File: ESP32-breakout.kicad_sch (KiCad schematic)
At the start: 39 parts, among them IC1 ESP32-S2-MINI-2U-N4, J1 UJ20-C-H-G-SMT-1-P16-TR, J2 Conn_01x03, J3 Conn_01x19, J4 Conn_01x19, Q2 Q_NMOS_DGS, SW3 SW_MEC_5E, SW4 SW_MEC_5E, U1 STUSB4500QTR, U2 TJA1051T-3, U4 TPSM33606S3QRDNRQ1, U7 MP9361DJ-LF-Z

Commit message: Finished V2 of the PCB
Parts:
- removed C10, C14: 2.2 uF, Capacitor_SMD:C_0603_1608Metric_Pad1.08x0.95mm_HandSolder, symbol Device:C_Small
- removed C11: 0.47 uF, Capacitor_SMD:C_0603_1608Metric_Pad1.08x0.95mm_HandSolder, symbol Device:C_Small
- removed C18: 4.7 uF, Capacitor_SMD:C_0603_1608Metric_Pad1.08x0.95mm_HandSolder, symbol Device:C_Small
- removed C19: 0.1 uF, Capacitor_SMD:C_0603_1608Metric_Pad1.08x0.95mm_HandSolder, symbol Device:C_Small
- removed C20: 1 uF, Capacitor_SMD:C_0603_1608Metric_Pad1.08x0.95mm_HandSolder, symbol Device:C_Small
- removed C21, C22: 22 uF, Capacitor_SMD:C_0603_1608Metric_Pad1.08x0.95mm_HandSolder, symbol Device:C_Small
- removed Q2: Q_NMOS_DGS, Package_TO_SOT_SMD:SOT-23-3, symbol Transistor_FET:Q_NMOS_DGS
- removed R14: 10k, Resistor_SMD:R_0603_1608Metric_Pad0.98x0.95mm_HandSolder, symbol Device:R_Small
- removed R15: 100k, Resistor_SMD:R_0603_1608Metric_Pad0.98x0.95mm_HandSolder, symbol Device:R_Small
- removed R16, R17: 4.7, Resistor_SMD:R_0603_1608Metric_Pad0.98x0.95mm_HandSolder, symbol Device:R_Small
- removed U1: STUSB4500QTR, Package_DFN_QFN:QFN-24-1EP_4x4mm_P0.5mm_EP2.7x2.7mm, symbol Interface_USB:STUSB4500QTR
- removed U4: TPSM33606S3QRDNRQ1, TPSM33606S3QRDNRQ1:TPSM33606S3QRDNRQ1, symbol TPSM33606S3QRDNRQ1:TPSM33606S3QRDNRQ1
- removed U7: MP9361DJ-LF-Z, Jayse_Footprints:TSOT23-6_MP9361_MNP, symbol 2026-06-30_18-02-43:MP9361DJ-LF-Z
- added C4, C5: 1 uF, Capacitor_SMD:C_01005_0402Metric, symbol Device:C_Small
- added D1: SBA0520CA_R1_00001, Package_TO_SOT_SMD:TSOT-23, symbol Device:D_Schottky_Dual_CommonCathode_AAK_Parallel
- added R2: 5.1k, Resistor_SMD:R_01005_0402Metric, symbol Device:R_Small
- added U1: SL6206-33NR, Package_TO_SOT_SMD:TSOT-23, symbol Regulator_Linear:LT1963AxST-3.3
- C1, C12, C13, C17, C2, C3: footprint Capacitor_SMD:C_0603_1608Metric_Pad1.08x0.95mm_HandSolder -> Capacitor_SMD:C_01005_0402Metric
- J3, J4: value Conn_01x19 -> Conn_01x20; footprint Connector_PinHeader_2.54mm:PinHeader_1x19_P2.54mm_Vertical -> Connector_PinHeader_2.54mm:PinHeader_1x20_P2.54mm_Vertical; symbol Connector_Generic:Conn_01x19 -> Connector_Generic:Conn_01x20
- R1: value 10k -> 5.1k; footprint Resistor_SMD:R_0603_1608Metric_Pad0.98x0.95mm_HandSolder -> Resistor_SMD:R_01005_0402Metric
- R10, R13: value 165 -> 165 Ω; footprint Resistor_SMD:R_0603_1608Metric_Pad0.98x0.95mm_HandSolder -> Resistor_SMD:R_01005_0402Metric
- R11, R12, R3, R4: footprint Resistor_SMD:R_0603_1608Metric_Pad0.98x0.95mm_HandSolder -> Resistor_SMD:R_01005_0402Metric
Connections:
- net +5VCAN is gone; now on net +5V: C2.1, U2.3 (VCC)
- net RESET_USB is gone; now on net GND: R1.2
- net +3.3V: now also C5.1, U1.3 (OUT)
- net +5V: now also C4.1, D1.3 (K), U1.1 (IN)
- net CIT_CAN+: now also J4.1 (Pin_1), R4.1; no longer J4.2 (Pin_2), R3.2
- net CIT_CAN-: now also J4.2 (Pin_2), R3.1; no longer J4.1 (Pin_1), R4.2
- net GND: now also J4.20 (Pin_20), C4.2, C5.2, R2.2, U1.2 (GND); no longer R1.1
- net VBUS: now also D1.1 (A)
- net at J2.1 (Pin_1): now also R4.2; no longer R4.1
- net at J2.3 (Pin_3): now also R3.2; no longer R3.1
- net CC1: no longer names the net of J1.A5 (CC1)
- net CC1: now also R1.1
- net CC2: no longer names the net of J1.B5 (CC2)
- net CC2: now also R2.1
- net SCL renamed GPIO 8
- net SDA renamed GPIO 7
- new net VIN: D1.2 (A), J3.20 (Pin_20)
- no-connect marks 11 -> 4
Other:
- removed sheet VBUS Power
- moved on the sheet: R3, R4

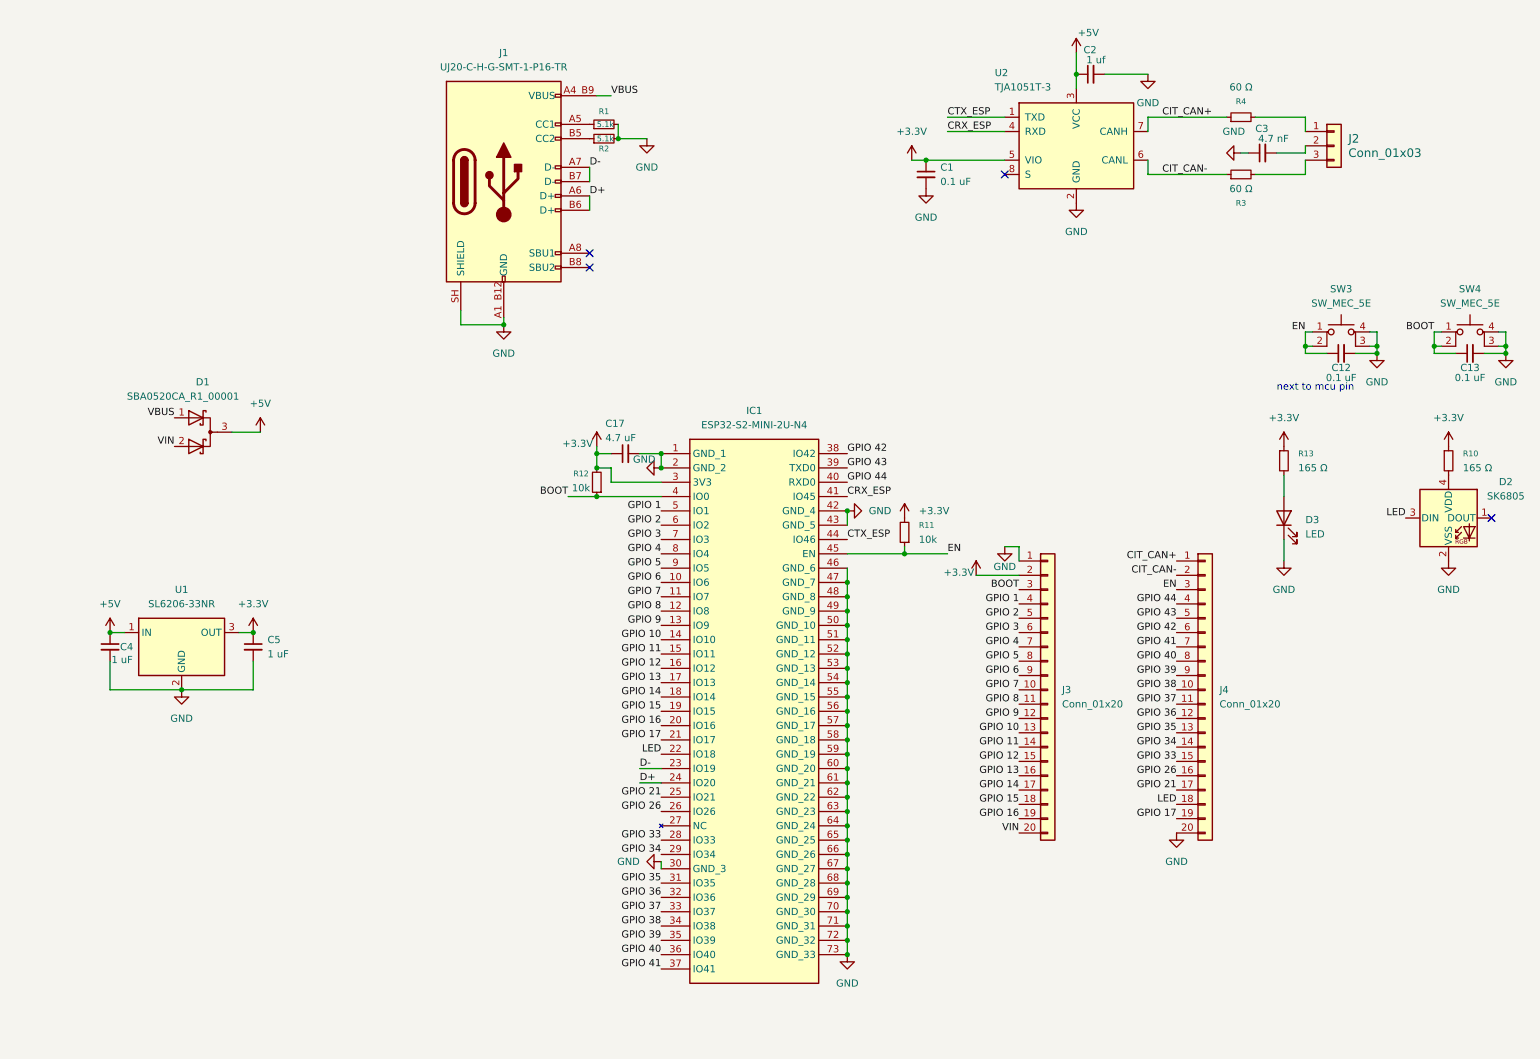
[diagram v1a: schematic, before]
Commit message: Changed power system and added ESD protection
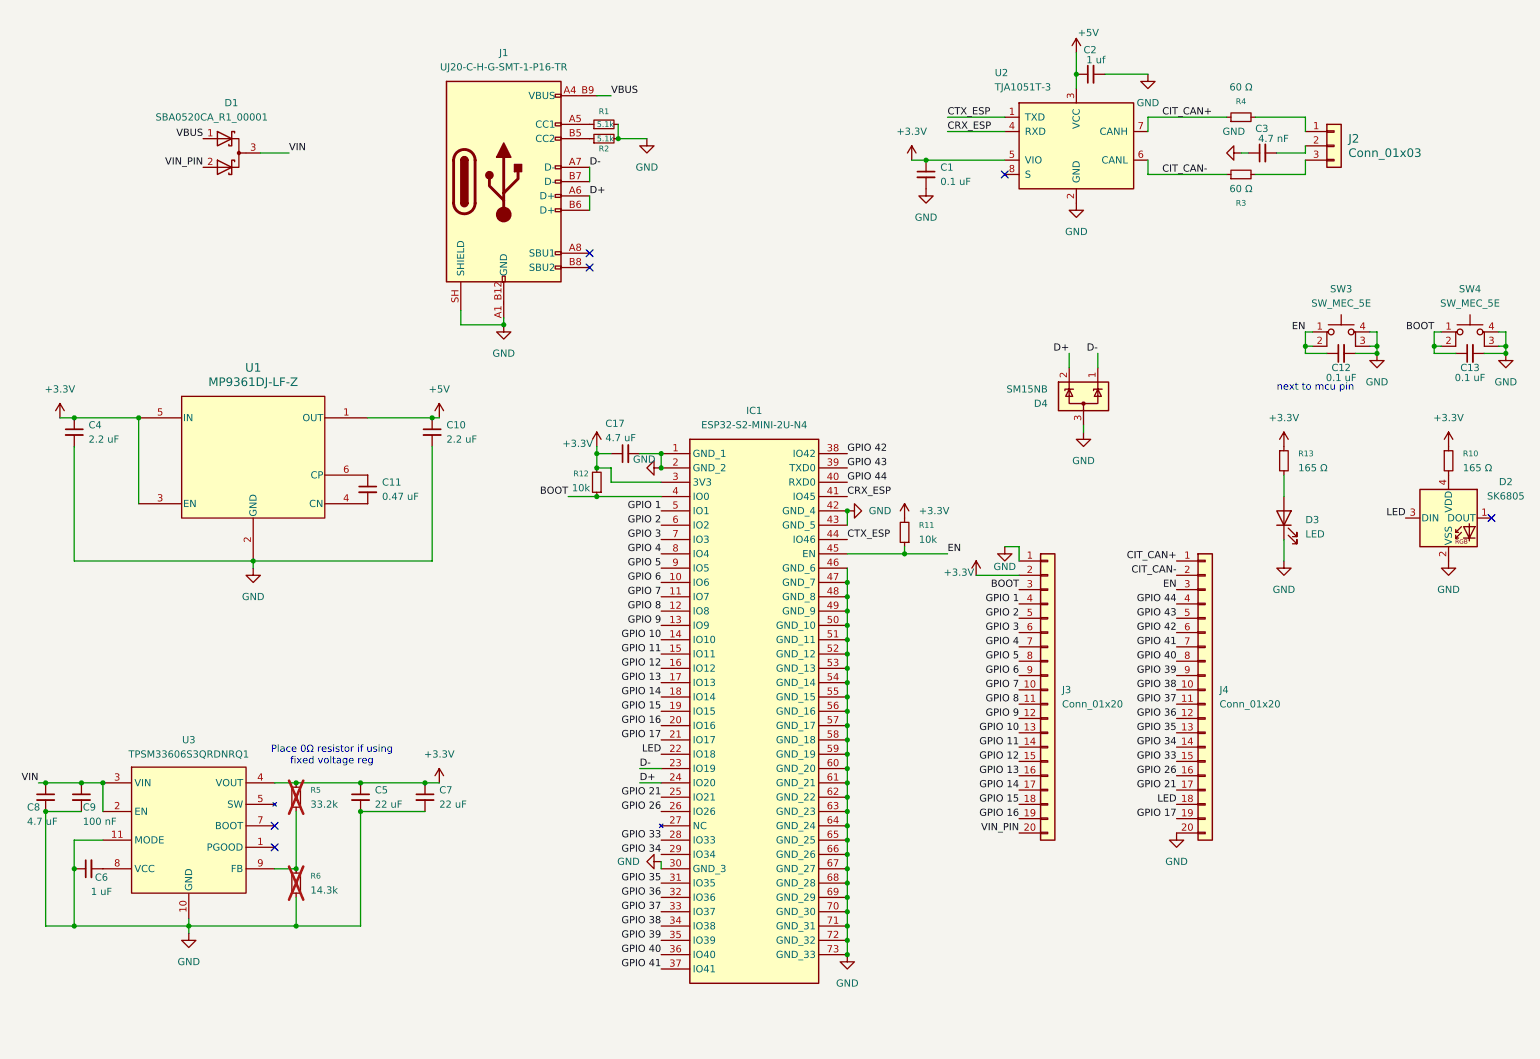
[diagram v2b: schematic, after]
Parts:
- removed U1: SL6206-33NR, Package_TO_SOT_SMD:TSOT-23, symbol Regulator_Linear:LT1963AxST-3.3
- added C10: 2.2 uF, Capacitor_SMD:C_01005_0402Metric, symbol Device:C_Small
- added C11: 0.47 uF, Capacitor_SMD:C_01005_0402Metric, symbol Device:C_Small
- added C6: 1 uF, Capacitor_SMD:C_01005_0402Metric, symbol Device:C_Small
- added C7: 22 uF, Capacitor_SMD:C_01005_0402Metric, symbol Device:C_Small
- added C8: 4.7 uF, Capacitor_SMD:C_01005_0402Metric, symbol Device:C_Small
- added C9: 100 nF, Capacitor_SMD:C_01005_0402Metric, symbol Device:C_Small
- added D4: SM15NB, Package_TO_SOT_SMD:SOT-23-3, symbol Power_Protection:ESDA5V3L
- added R5: 33.2k, Resistor_SMD:R_01005_0402Metric, symbol Device:R_Small
- added R6: 14.3k, Resistor_SMD:R_01005_0402Metric, symbol Device:R_Small
- added U1: MP9361DJ-LF-Z, Jayse_Footprints:TSOT23-6_MP9361_MNP, symbol 2026-06-30_18-02-43:MP9361DJ-LF-Z
- added U3: TPSM33606S3QRDNRQ1, TPSM33606S3QRDNRQ1:TPSM33606S3QRDNRQ1, symbol TPSM33606S3QRDNRQ1:TPSM33606S3QRDNRQ1
- C4: value 1 uF -> 2.2 uF
- C5: value 1 uF -> 22 uF
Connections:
- net +3.3V: now also C4.1, C7.1, R5.1, U1.3 (EN), U1.5 (IN), U3.4 (VOUT)
- net +5V: now also C10.1, U1.1 (OUT); no longer C4.1, D1.3 (K)
- net D+: now also D4.2 (K)
- net D-: now also D4.1 (K)
- net GND: now also C10.2, C6.1, C7.2, C8.2, C9.2, D4.3 (A), R6.2, U1.2 (GND), U3.10 (GND), U3.11 (MODE)
- net VIN: now also D1.3 (K), C8.1, C9.1, U3.2 (EN), U3.3 (VIN); no longer D1.2 (A), J3.20 (Pin_20)
- new net: C11.1, U1.6 (CP)
- new net: C11.2, U1.4 (CN)
- new net: R5.2, R6.1, U3.9 (FB)
- new net: U3.5 (SW), U3.6 (SW)
- new net: C6.2, U3.8 (VCC)
- new net VIN_PIN: D1.2 (A), J3.20 (Pin_20)
- no-connect marks 4 -> 6
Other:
- note added: "Place 0Ω resistor if using fixed voltage reg"
- moved on the sheet: C5, D1

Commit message: Changed capacitors and ESD diodes, began revisions
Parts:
- removed D4: SM15NB, Package_TO_SOT_SMD:SOT-23-3, symbol Power_Protection:ESDA5V3L
- added C14, C15: 1 nF, Capacitor_SMD:C_0402_1005Metric, symbol Device:C_Small
- added D5, D6, D7, D8: TPD1E05U06QDPYRQ1, Diode_SMD:D_0603_1608Metric, symbol Device:D_TVS
- C1, C10, C11, C12, C13, C17, C2, C3, C4, C5, C6, C7: footprint Capacitor_SMD:C_01005_0402Metric -> Capacitor_SMD:C_0402_1005Metric
- C8: footprint Capacitor_SMD:C_01005_0402Metric -> Capacitor_SMD:C_1206_3216Metric
- C9: value 100 nF -> 4.7 uF; footprint Capacitor_SMD:C_01005_0402Metric -> Capacitor_SMD:C_1206_3216Metric
- R1, R10, R11, R12, R13, R2, R3, R4, R5, R6: footprint Resistor_SMD:R_01005_0402Metric -> Resistor_SMD:R_0402_1005Metric
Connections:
- net GPIO 34 is gone; now on net LED: IC1.29 (IO34), J4.14 (Pin_14)
- net +3.3V: now also C15.1
- net CIT_CAN+: now also D7.1 (A1)
- net CIT_CAN-: now also D8.1 (A1)
- net D+: now also D5.1 (A1)
- net D-: now also D6.1 (A1)
- net GND: now also C14.2, C15.2, D5.2 (A2), D6.2 (A2), D7.2 (A2), D8.2 (A2)
- net LED: no longer IC1.22 (IO18), J4.18 (Pin_18)
- net VBUS: now also D1.2 (A); no longer D1.1 (A)
- net VIN: now also C14.1
- net VIN_PIN: now also D1.1 (A); no longer D1.2 (A)
- new net GPIO 18: IC1.22 (IO18), J4.18 (Pin_18)
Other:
- moved on the sheet: C5, C6, C7, C8, C9, R5, R6, U3
